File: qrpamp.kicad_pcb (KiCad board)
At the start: 2 copper layers, 144.8 x 85.1 mm, 117 parts, among them K1 BAND3_IN, K2 BAND2_IN, K3 BAND1_IN, K4 BAND3_OUT, K5 BAND2_OUT, K6 BAND1_OUT, K7 ANT_RLY, P1 PWR, P2 PWR_SW, P3 SWD, P4 ANT, P5 RADIO, P6 PTT_IN, P7 TP, P8 NAV_BUTTON, Q1 MMBT6427, Q10 MMBF170, Q11 MMBF170, Q2 MMBF170, Q3 IRF510, Q4 IRF510, Q6 MMBF170, Q9 MMBF170, SW1 SW_PUSH, T1 8:8, T2 8:8, T3 2:3, T4 12:1, T5 1:12, U1 LM7805, U2 LM3940, U3 LCD-2x16, U4 STM32F401xB/C-LQFP

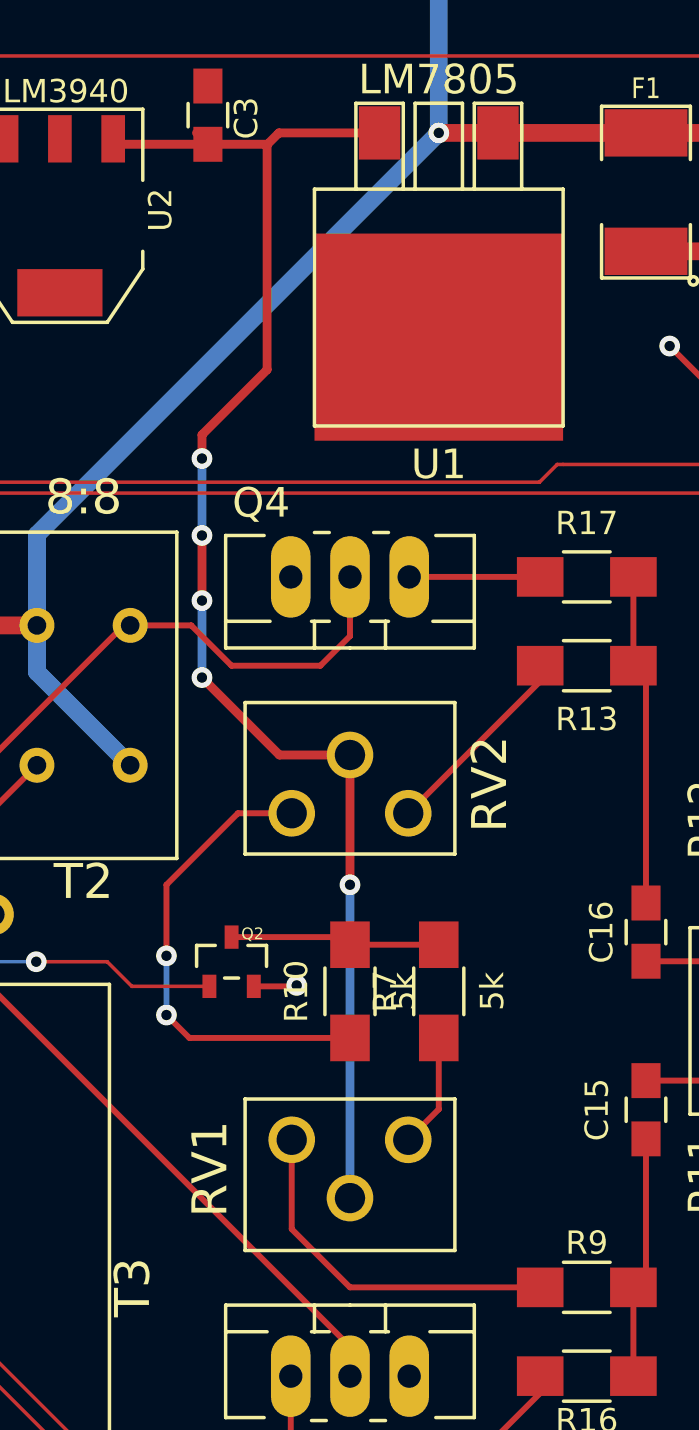
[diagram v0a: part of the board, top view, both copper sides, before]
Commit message: Fixes #5: bad bias pot pin numbers
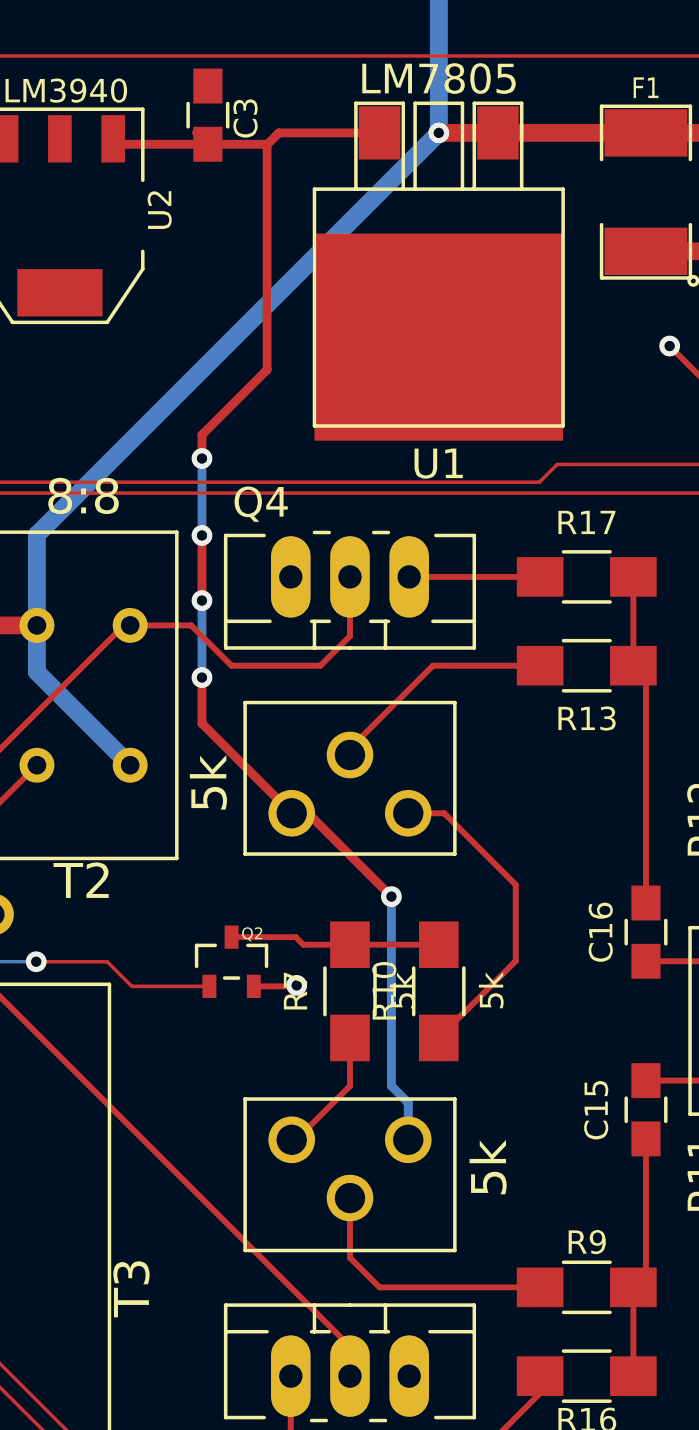
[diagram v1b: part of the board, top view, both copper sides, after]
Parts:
- moved R10 3.81 mm to (175.3, 94.0)
- moved R7 3.81 mm to (171.4, 94.0)
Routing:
- net Net-(R10-Pad1): track 20.5 -> 13.8 mm, vias 2 -> 0
- net Net-(R9-Pad2): track 15.5 -> 11.2 mm
- net +5V: track 63.2 -> 60.4 mm
- net Net-(R13-Pad2): track 8.67 -> 10.6 mm
- net Net-(R7-Pad1): track 4.91 -> 5.52 mm

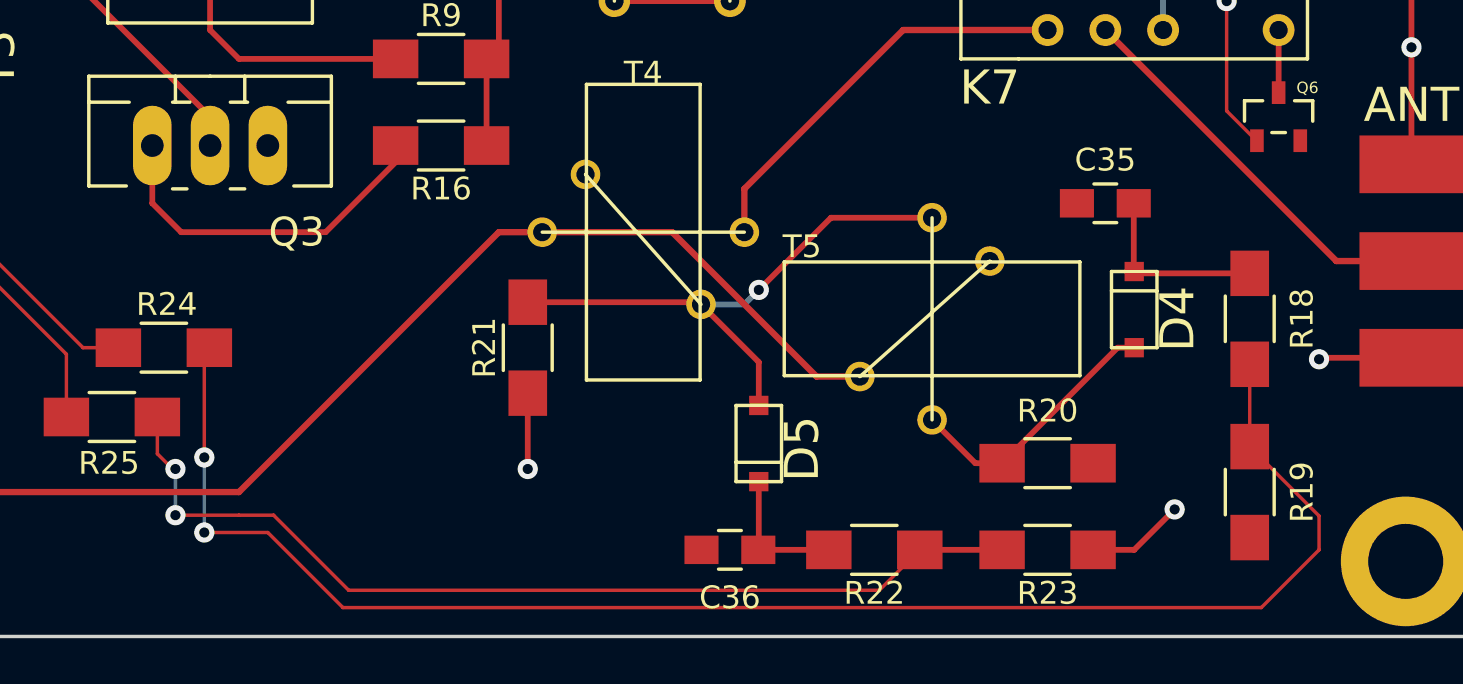
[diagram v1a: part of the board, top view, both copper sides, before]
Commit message: Fixes #6: removes SWR measurement voltage divider
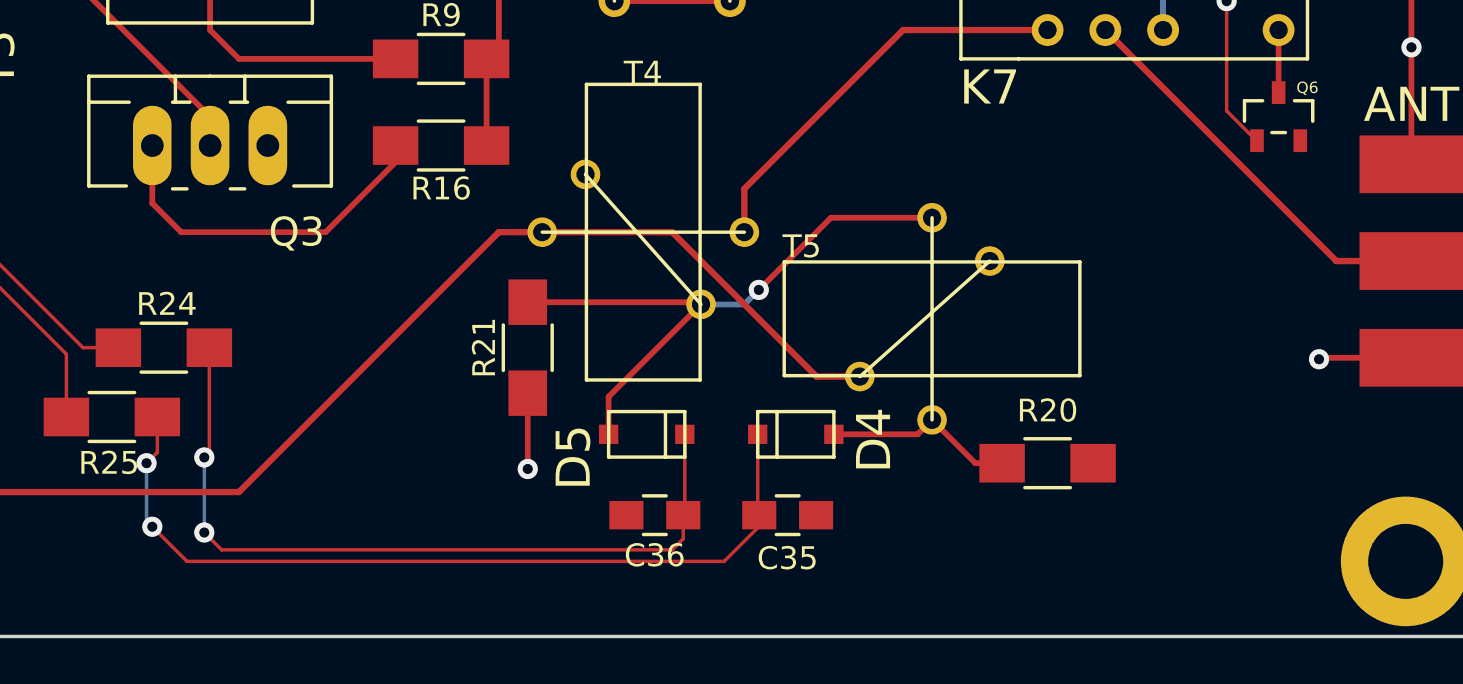
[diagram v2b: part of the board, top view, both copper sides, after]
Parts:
- removed R18, R22: 15k, Resistors_SMD:R_1206_HandSoldering
- removed R19, R23: 1k, Resistors_SMD:R_1206_HandSoldering
- moved C35 19.6 mm to (196.8, 126.7), turned to 0 degrees
- moved D4 13.7 mm to (198.9, 123.2), turned to 180 degrees
- moved D5 6.73 mm to (189.0, 123.2), turned to 0 degrees
- moved C36 3.64 mm to (191.0, 126.7)
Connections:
- C35 pad 1: Net-(C35-Pad1) -> /Microcontroller/mcu_swr_ref
- C36 pad 1: Net-(C36-Pad1) -> /Microcontroller/mcu_swr_fwd
- D4 pad 2: Net-(C35-Pad1) -> /Microcontroller/mcu_swr_ref
- D5 pad 2: Net-(C36-Pad1) -> /Microcontroller/mcu_swr_fwd
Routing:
- net /Microcontroller/mcu_swr_fwd: track 69.1 -> 34.7 mm
- net Net-(C35-Pad1): track 8.12 -> 0.00 mm
- net Net-(C36-Pad1): track 6.11 -> 0.00 mm
- net /Microcontroller/mcu_swr_ref: track 43.2 -> 37.2 mm
- net GND: track 60.7 -> 56.3 mm, vias 13 -> 12
- net Net-(D4-Pad1): track 11.8 -> 8.45 mm
- net Net-(D5-Pad1): track 24.9 -> 26.7 mm

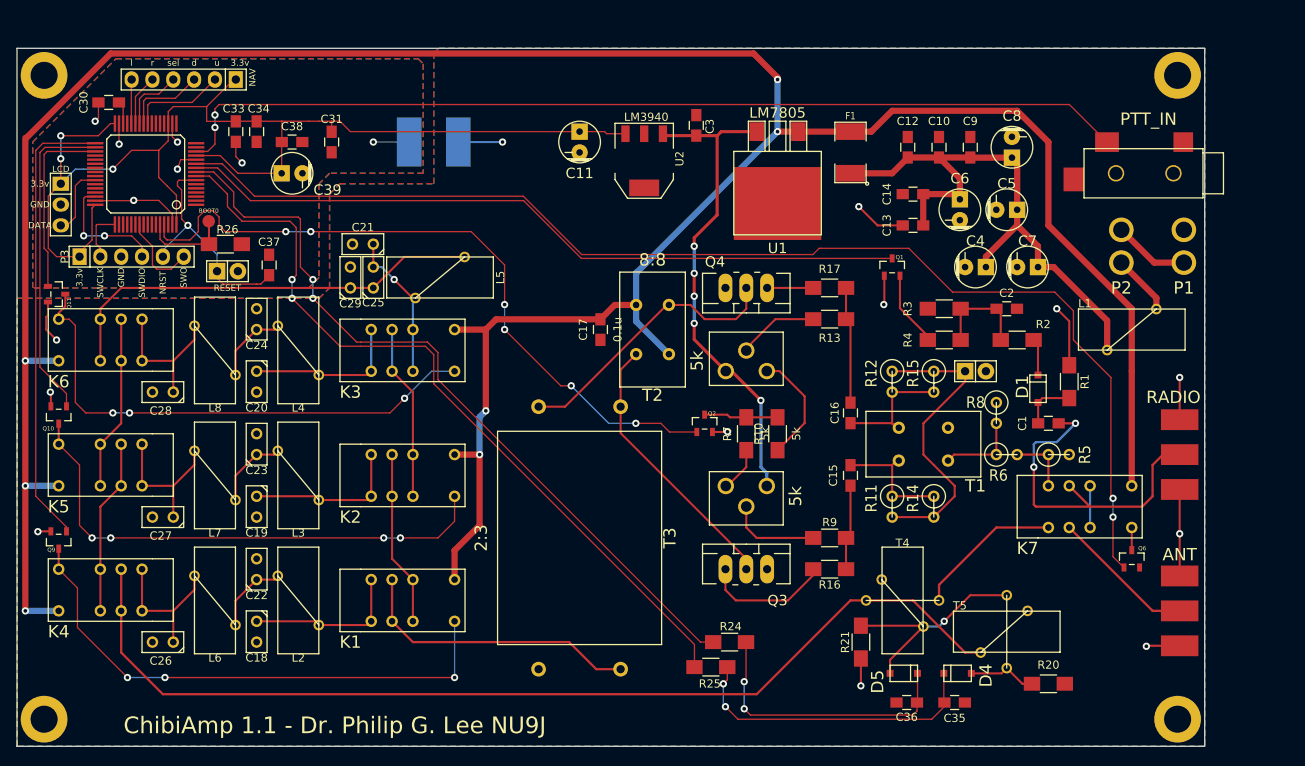
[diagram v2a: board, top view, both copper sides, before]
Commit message: Closes #3: extend SOT23 pads
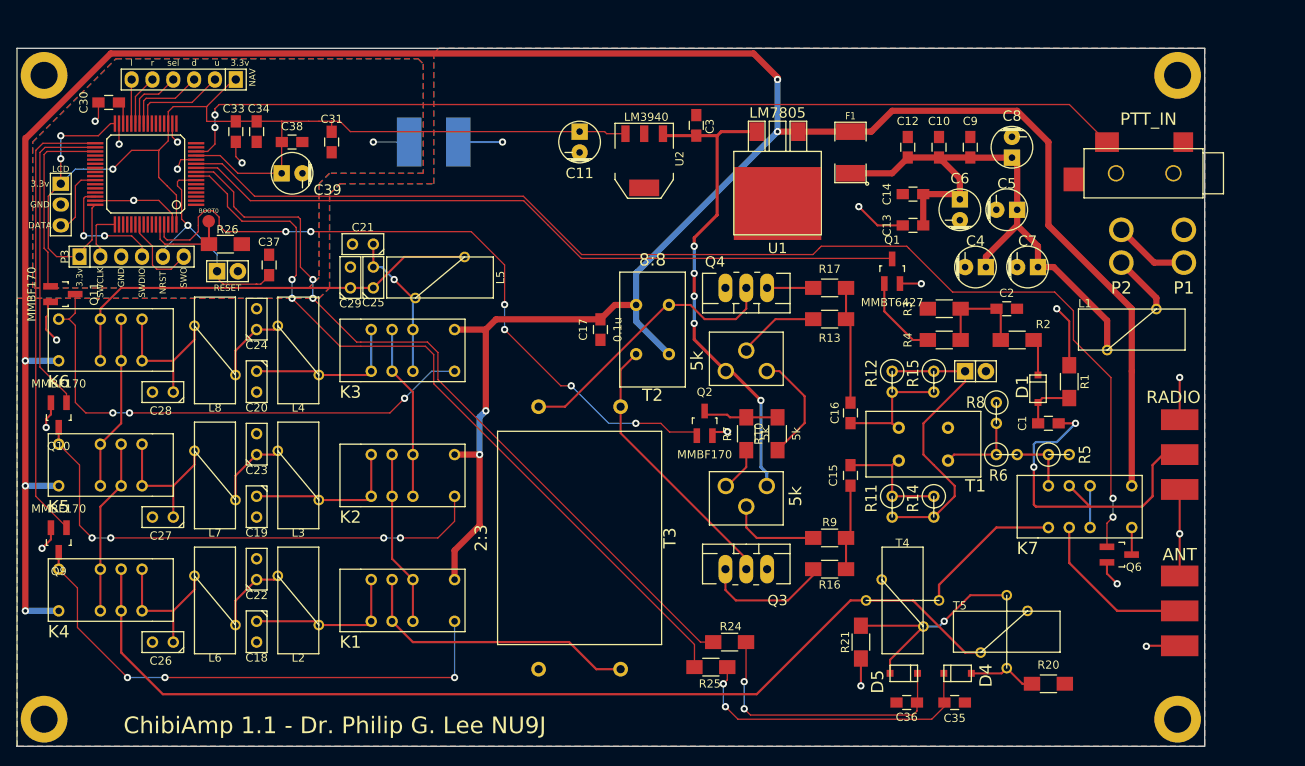
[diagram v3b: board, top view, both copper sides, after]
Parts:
- Q1: footprint Transistors_SMD:sot23 -> nu9j-footprints:SOT-23-EBC_HandSoldering
- Q10, Q11, Q2, Q6, Q9: footprint nu9j-footprints:sot23-DGS -> nu9j-footprints:SOT-23-DGS_HandSoldering
- moved Q6 1.61 mm to (216.9, 108.7), turned to 270 degrees
- moved Q11 0.76 mm to (88.1, 77.0)
- moved Q1 0.51 mm to (189.2, 74.2)
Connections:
- R4 pad 1: Net-(Q1-Pad2) -> Net-(Q1-Padb)
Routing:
- net Net-(Q1-Padb): track 0.00 -> 10.6 mm
- net Net-(Q1-Pad2): track 9.24 -> 0.00 mm
- net GND: track 56.3 -> 61.4 mm, vias 12 -> 13
- net /RF In/Out/ant_sw_rly: track 148.8 -> 146.3 mm
- net Net-(K7-Pad9): track 17.7 -> 20.2 mm
- net Net-(K7-Pad12): track 2.75 -> 3.31 mm

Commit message: Fixes #7: board to 6x3.5 inches
Have not yet moved all the parts around.
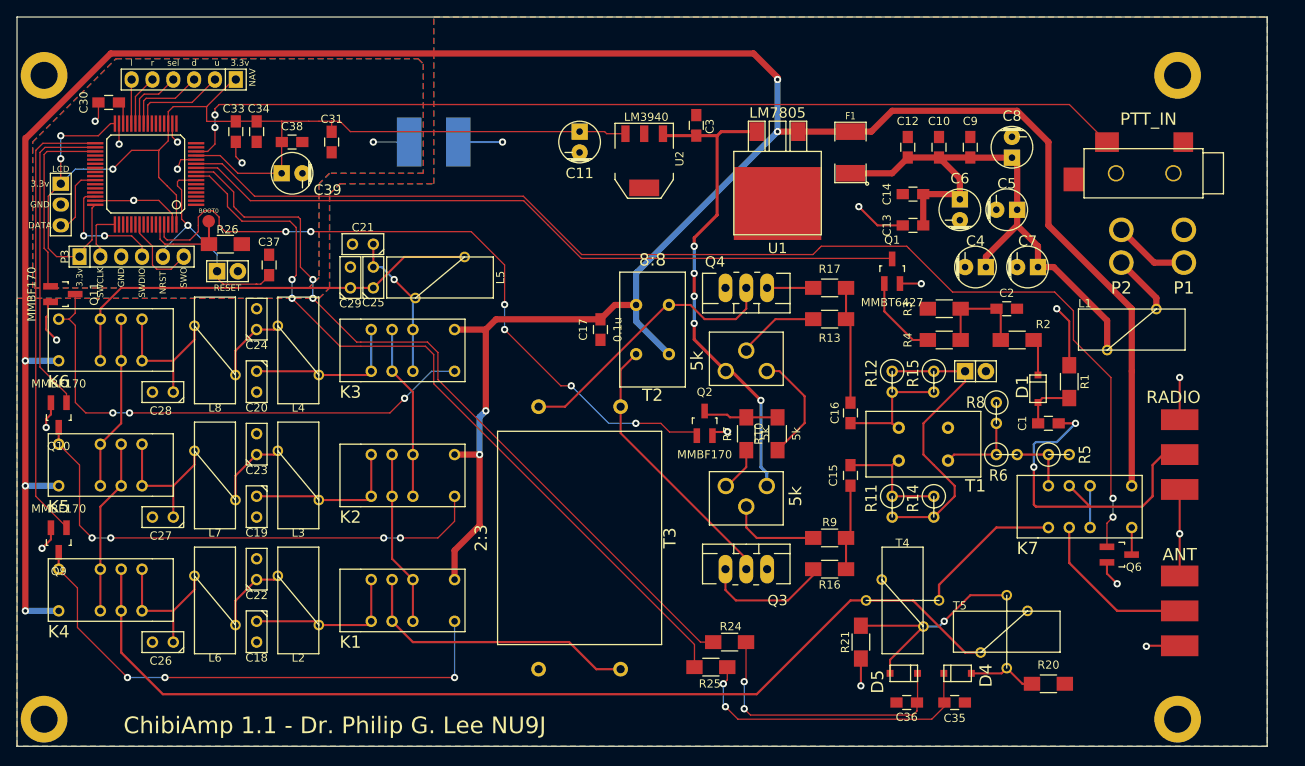
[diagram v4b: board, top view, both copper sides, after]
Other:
- board size 144.8 x 85.1 mm -> 152.4 x 88.9 mm
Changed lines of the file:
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@@
     (area 82.474999 46.914999 227.405001 132.155001)
     (thickness 1.6)
-    (drawings 25)
+    (drawings 26)
     (tracks 693)
     (zones 0)
@@
     )
   )
+  (gr_line (start 82.55 43.18) (end 82.55 132.08) (angle 90) (layer Edge.Cuts) (width 0.15))
+  (gr_line (start 234.95 43.18) (end 82.55 43.18) (angle 90) (layer Edge.Cuts) (width 0.15))
+  (gr_line (start 227.33 132.08) (end 234.95 132.08) (angle 90) (layer Edge.Cuts) (width 0.15))
+  (gr_line (start 234.95 132.08) (end 234.95 43.18) (angle 90) (layer Edge.Cuts) (width 0.15))
   (gr_text "Copyright Philip G. Lee 2015.\nLicensed under the TAPR\nOpen Hardware License\nversion 1.0 (www.tapr.org/OHL)." (at 150.876 107.95) (layer B.SilkS)
     (effects (font (size 1 1) (thickness 0.2)) (justify mirror))
@@
     (effects (font (size 0.762 0.762) (thickness 0.1524)))
   )
-  (gr_line (start 227.33 46.99) (end 227.33 132.08) (angle 90) (layer Edge.Cuts) (width 0.15))
-  (gr_line (start 82.55 46.99) (end 82.55 132.08) (angle 90) (layer Edge.Cuts) (width 0.15))
   (gr_text BOOT0 (at 105.918 66.802) (layer F.SilkS)
     (effects (font (size 0.508 0.508) (thickness 0.1016)))
@@
     (effects (font (size 2.032 2.032) (thickness 0.3556)))
   )
-  (gr_line (start 227.33 46.99) (end 82.55 46.99) (angle 90) (layer Edge.Cuts) (width 0.15))
   (gr_line (start 82.55 132.08) (end 227.33 132.08) (angle 90) (layer Edge.Cuts) (width 0.15))
   (segment (start 217.4875 110.27664) (end 217.46464 110.27664) (width 0.1524) (layer F.Cu) (net 0))
@@
     (polygon
       (pts
-        (xy 227.33 132.08) (xy 82.55 132.08) (xy 82.55 77.47) (xy 119.38 77.47) (xy 120.65 76.2)
-        (xy 120.65 64.77) (xy 121.92 63.5) (xy 133.35 63.5) (xy 133.35 47.625) (xy 133.985 46.99)
-        (xy 227.33 46.99)
+        (xy 234.95 132.08) (xy 82.55 132.08) (xy 82.55 77.47) (xy 119.38 77.47) (xy 120.65 76.2)
+        (xy 120.65 64.77) (xy 121.92 63.5) (xy 133.35 63.5) (xy 133.35 47.625) (xy 133.35 43.18)
+        (xy 234.95 43.18)
       )
     )
@@
     (polygon
       (pts
-        (xy 227.33 132.08) (xy 82.55 132.08) (xy 82.55 77.47) (xy 119.38 77.47) (xy 120.65 76.2)
-        (xy 120.65 64.77) (xy 121.92 63.5) (xy 133.35 63.5) (xy 133.35 47.625) (xy 133.985 46.99)
-        (xy 227.33 46.99)
+        (xy 234.95 132.08) (xy 82.55 132.08) (xy 82.55 77.47) (xy 119.38 77.47) (xy 120.65 76.2)
+        (xy 120.65 64.77) (xy 121.92 63.5) (xy 133.35 63.5) (xy 133.35 47.625) (xy 133.35 43.18)
+        (xy 234.95 43.18)
       )
     )
